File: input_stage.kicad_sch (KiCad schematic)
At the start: 35 parts, among them K1 EE2-3NUX, Q1 2N7002, U1 REF5030AD, U2 TL072, U6 NCS21802DMR2G, U7 CD4051B

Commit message: tiny.
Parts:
- added R29: 100k, Resistor_SMD:R_0603_1608Metric_Pad0.98x0.95mm_HandSolder, symbol Device:R_US
- R1, R10, R11, R2, R3, R4, R5, R7, R8, R9: footprint (none) -> Resistor_SMD:R_1206_3216Metric_Pad1.30x1.75mm_HandSolder
- R12, R13, R14, R15, R16, R17, R22, R23, R24, R25, R26, R27, R6: footprint (none) -> Resistor_SMD:R_0603_1608Metric_Pad0.98x0.95mm_HandSolder
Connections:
- net GND: now also R29.1
- net at R3.1: now also R5.1; no longer R2.1
- net at R8.1: now also R10.1; no longer R2.2
- net at Q1.1 (G), R14.1: now also R29.2
- net at R4.1: now also R3.2; no longer R5.1
- net at R5.2: now also R7.1; no longer R11.1
- net at R7.2: now also R9.2; no longer R8.2
- net at R9.1: now also R8.2; no longer R3.2
- net at R10.2: now also R11.1; no longer R9.2
- net at R4.2: now also R2.2; no longer R10.1
- net at R1.2: now also R2.1; no longer R7.1
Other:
- moved on the sheet: R14

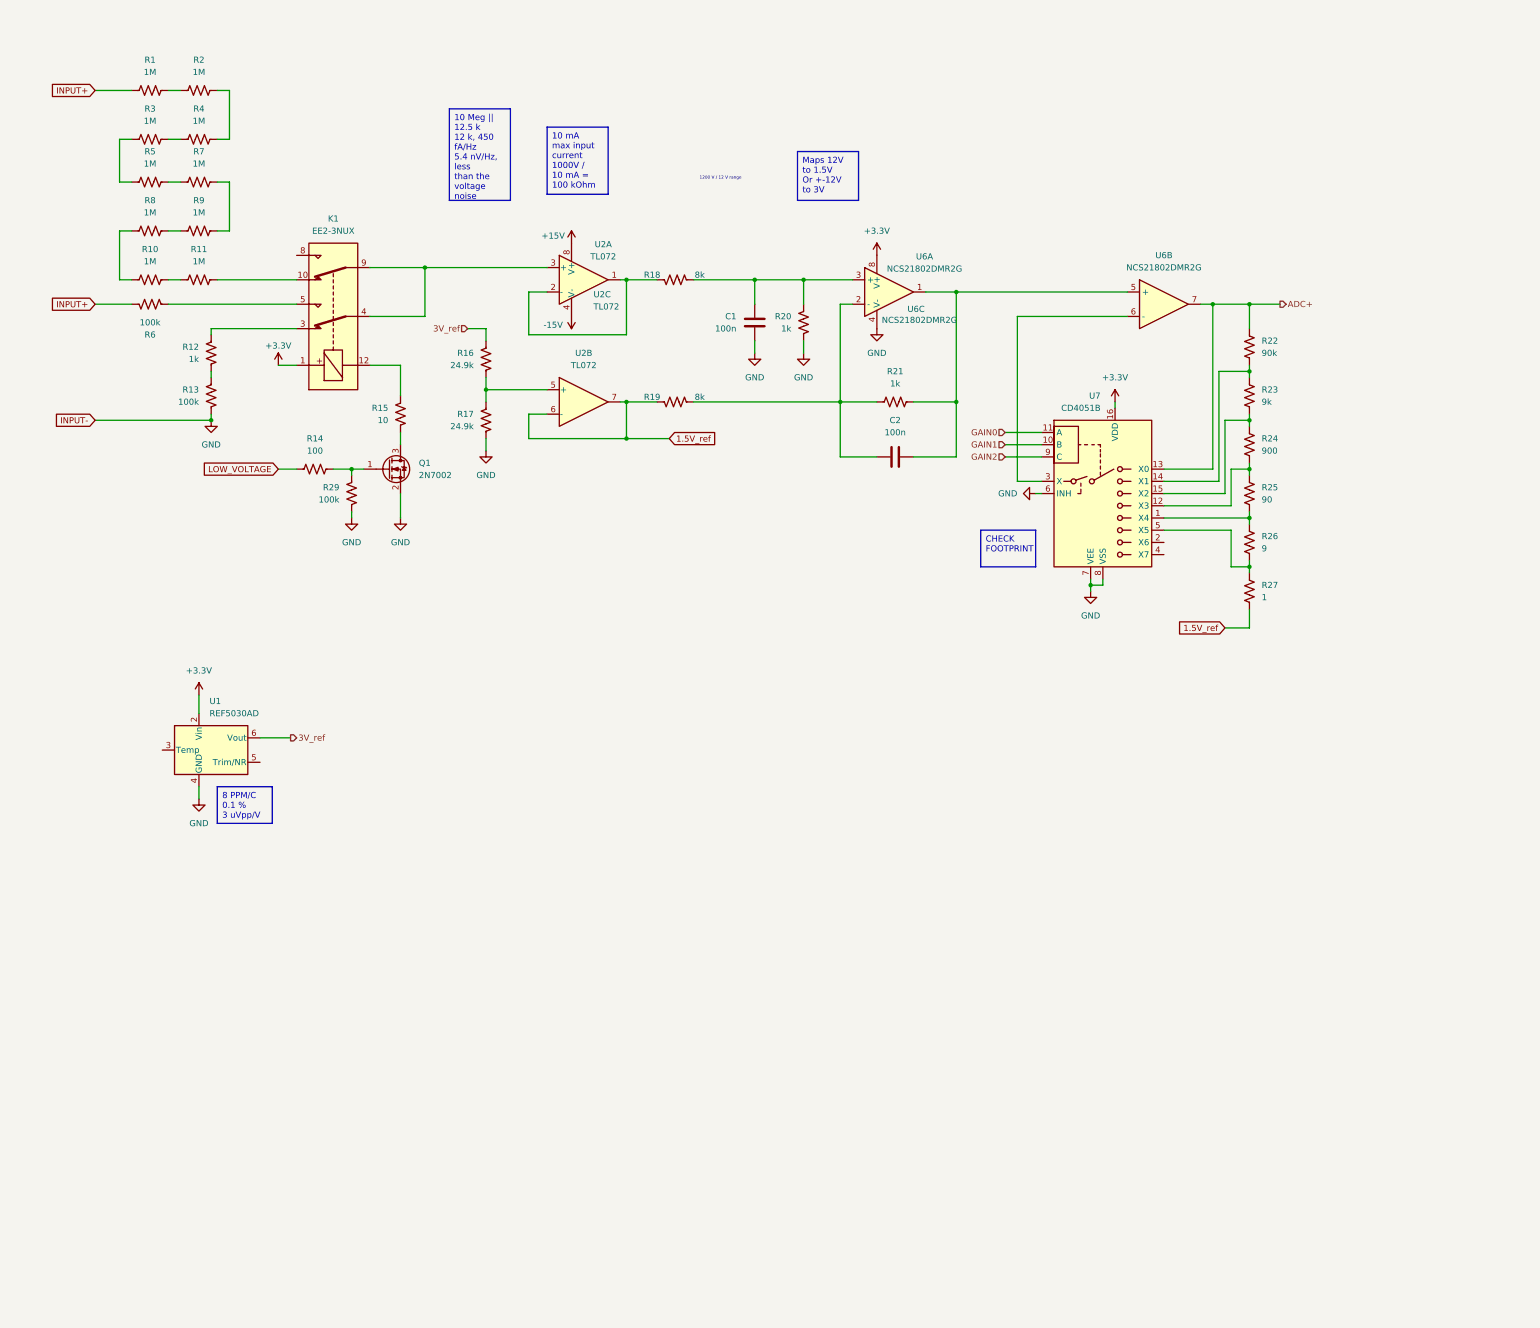
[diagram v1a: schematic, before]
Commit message: Added temperature, ref trimming and range selection resisitors.
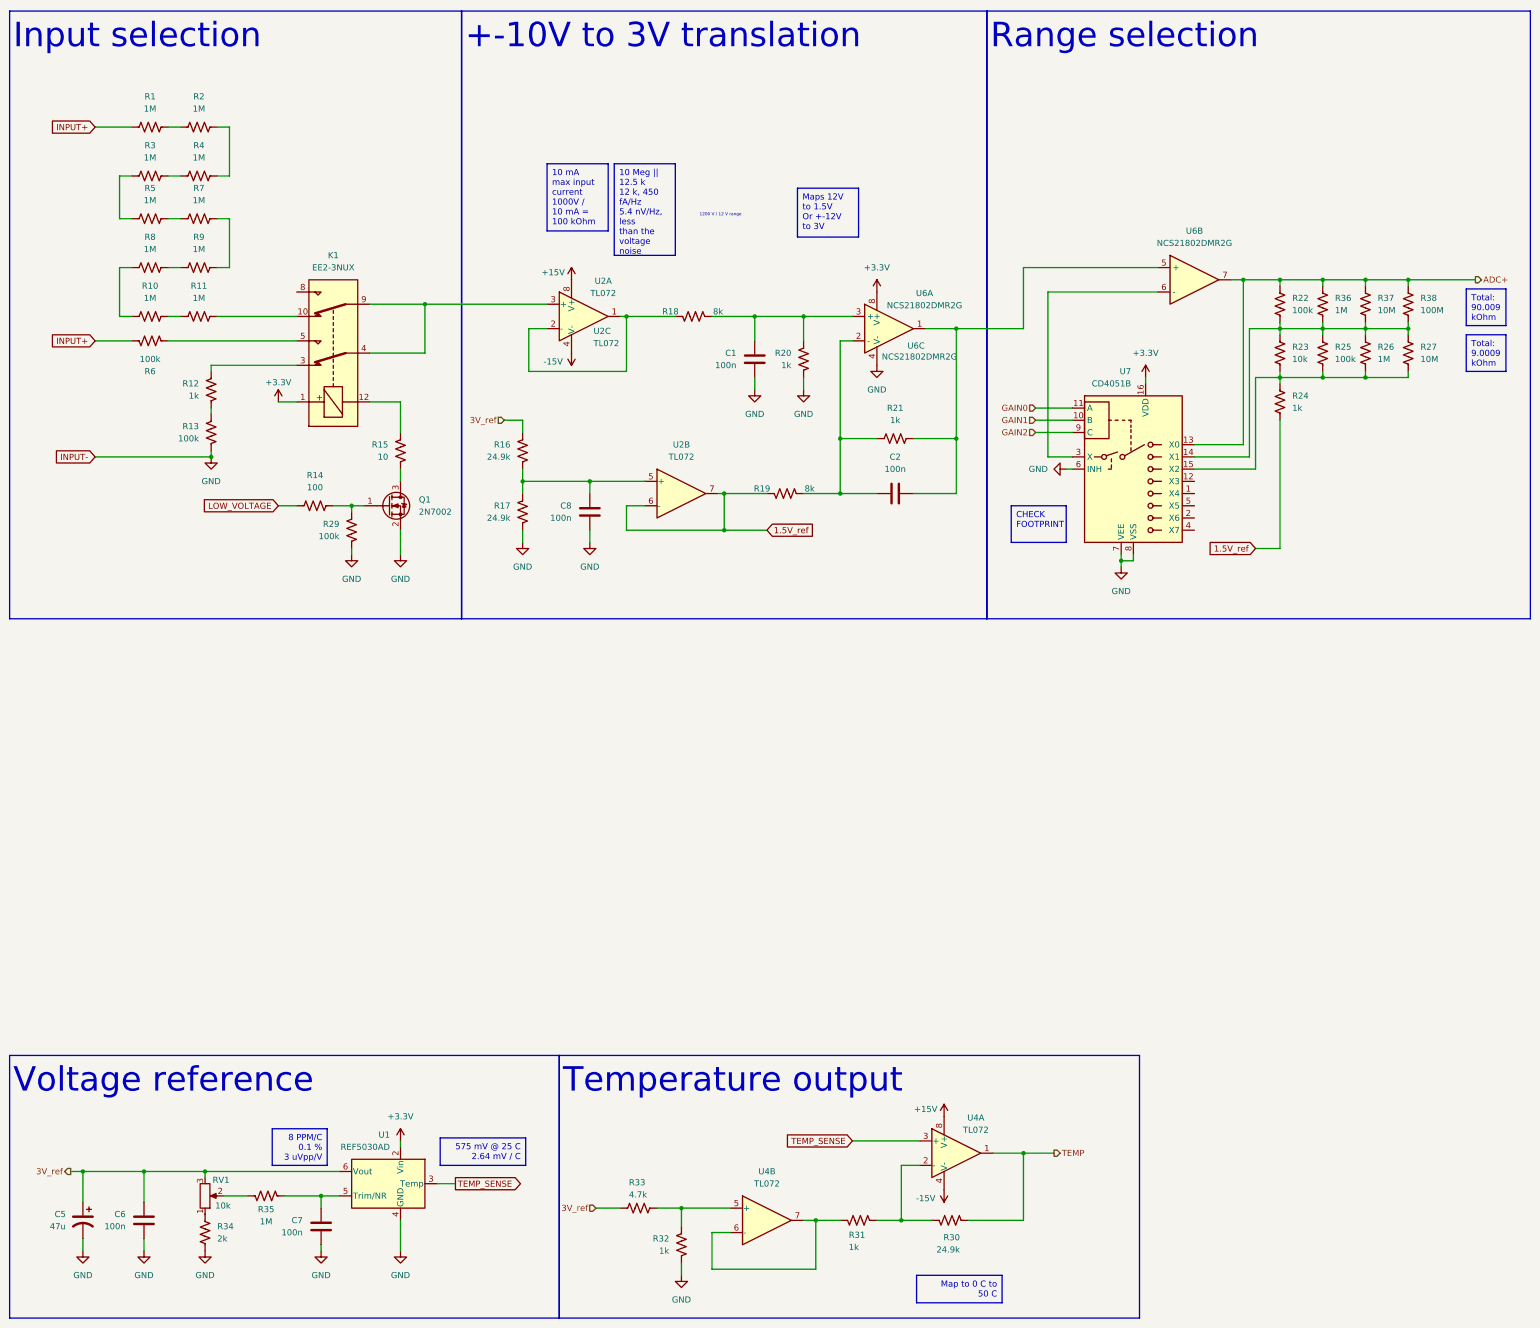
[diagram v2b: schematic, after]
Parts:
- added C5: 47u, Capacitor_THT:CP_Radial_D5.0mm_P2.00mm, symbol Device:C_Polarized_US
- added C6, C7, C8: 100n, Capacitor_SMD:C_0603_1608Metric_Pad1.08x0.95mm_HandSolder, symbol Device:C
- added R30: 24.9k, Resistor_SMD:R_0603_1608Metric_Pad0.98x0.95mm_HandSolder, symbol Device:R_US
- added R31, R32: 1k, Resistor_SMD:R_0603_1608Metric_Pad0.98x0.95mm_HandSolder, symbol Device:R_US
- added R33: 4.7k, Resistor_SMD:R_0603_1608Metric_Pad0.98x0.95mm_HandSolder, symbol Device:R_US
- added R34: 2k, Resistor_SMD:R_0603_1608Metric_Pad0.98x0.95mm_HandSolder, symbol Device:R_US
- added R35, R36: 1M, Resistor_SMD:R_0603_1608Metric_Pad0.98x0.95mm_HandSolder, symbol Device:R_US
- added R37: 10M, Resistor_SMD:R_0603_1608Metric_Pad0.98x0.95mm_HandSolder, symbol Device:R_US
- added R38: 100M, Resistor_SMD:R_0603_1608Metric_Pad0.98x0.95mm_HandSolder, symbol Device:R_US
- added RV1: 10k, Potentiometer_THT:Potentiometer_Bourns_3296W_Vertical, symbol Device:R_Potentiometer
- added U4: TL072, Package_SO:SOIC-8_3.9x4.9mm_P1.27mm, symbol Amplifier_Operational:TL072
- R22: value 90k -> 100k
- R23: value 9k -> 10k
- R24: value 900 -> 1k
- R25: value 90 -> 100k
- R26: value 9 -> 1M
- R27: value 1 -> 10M
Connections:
- net +15V: now also U4.8 (V+)
- net -15V: now also U4.4 (V-)
- net 1.5V_ref: now also R24.1; no longer R27.1
- net 3V_ref: now also C5.1, C6.2, R33.1, RV1.3
- net ADC+: now also R36.2, R37.2, R38.2
- net GND: now also C5.2, C6.1, C7.1, C8.1, R32.1, R34.1
- net at R22.1, R23.2, U7.14 (X1): now also R25.2, R26.2, R27.2, R36.1, R37.1, R38.1
- net at R23.1, R24.2, U7.15 (X2): now also R25.1, R26.1, R27.1
- net at R16.1, R17.2, U2.5 (+): now also C8.2
- net TEMP_SENSE: now reaches U1.3 (Temp)
- net TEMP_SENSE: now also U4.3 (+)
- net at U1.5 (Trim/NR): now also C7.2, R35.1
- new net: R30.2, R31.2, U4.2 (-)
- new net: R32.2, R33.2, U4.5 (+)
- new net: R31.1, U4.6 (-), U4.7
- new net: R34.2, RV1.1
- new net: R35.2, RV1.2
- new net TEMP: R30.1, U4.1
- now unconnected: U7.1 (X4), U7.12 (X3), U7.5 (X5)
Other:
- note added: "+-10V to 3V translation"
- note added: "Input selection"
- note added: "Range selection"
- note added: "Temperature output"
- note added: "Voltage reference"
- moved on the sheet: C1, C2, K1, Q1, R1, R10, R11, R12, R13, R14, R15, R16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

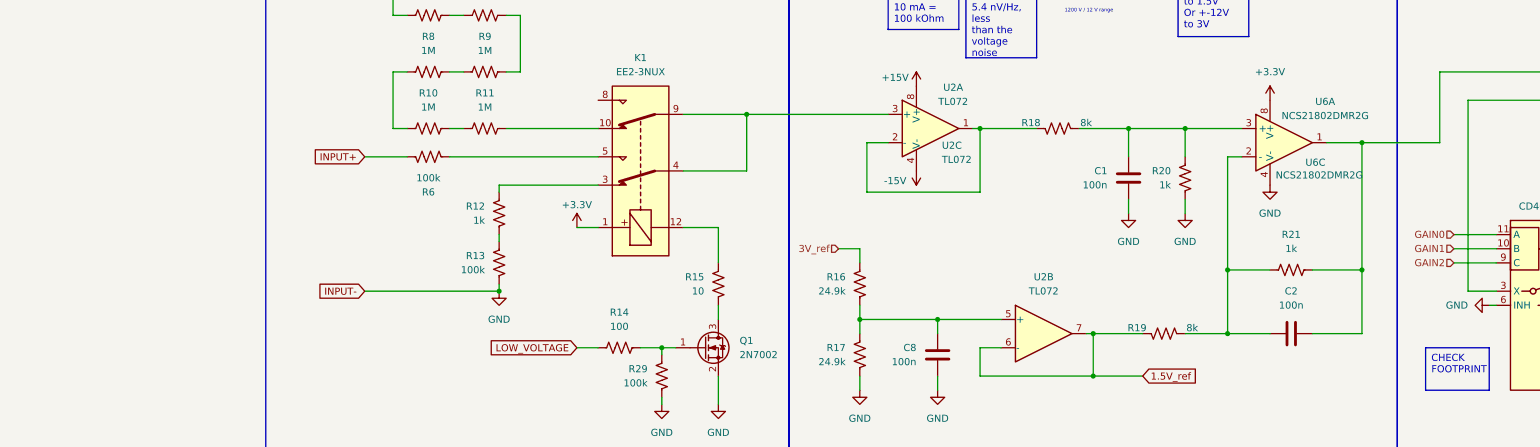
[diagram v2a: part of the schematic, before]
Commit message: Fixed diff amp.
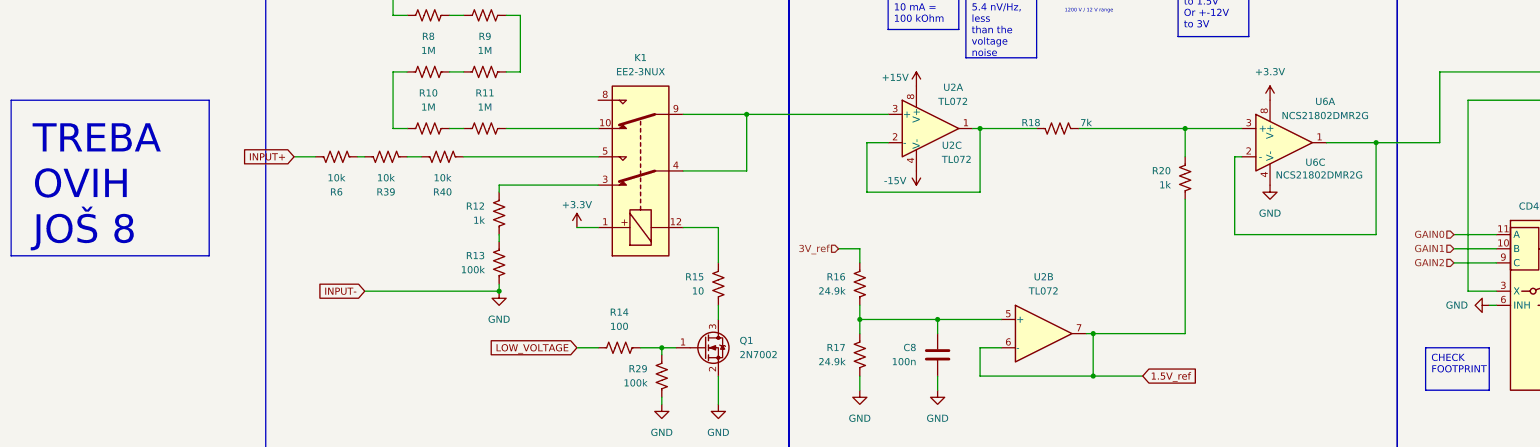
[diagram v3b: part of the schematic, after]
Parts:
- removed C1, C2: 100n, Capacitor_SMD:C_0603_1608Metric_Pad1.08x0.95mm_HandSolder, symbol Device:C
- removed R19: 8k, Resistor_SMD:R_0603_1608Metric_Pad0.98x0.95mm_HandSolder, symbol Device:R_US
- removed R21: 1k, Resistor_SMD:R_0603_1608Metric_Pad0.98x0.95mm_HandSolder, symbol Device:R_US
- added R39, R40: 10k, Resistor_SMD:R_0603_1608Metric_Pad0.98x0.95mm_HandSolder, symbol Device:R_US
- R18: value 8k -> 7k
- R6: value 100k -> 10k
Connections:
- net 1.5V_ref: now also R20.1
- net GND: no longer R20.1
- net at U6.1, U6.5 (+): now also U6.2 (-)
- net at K1.5: now also R40.1; no longer R6.1
- new net: R39.1, R40.2
- new net: R39.2, R6.1
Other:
- moved on the sheet: R6

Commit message: Recheck
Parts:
- added R19, R21, R41, R42, R43, R44, R45: 100k, Resistor_SMD:R_0603_1608Metric_Pad0.98x0.95mm_HandSolder, symbol Device:R_US
- R39, R40, R6: value 10k -> 100k
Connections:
- net INPUT+: now also R45.2; no longer R6.2
- net at R40.1: now also R21.1; no longer K1.5
- net at R39.1: now also R21.2; no longer R40.2
- net at R6.1: now also K1.8; no longer R39.2
- new net: R19.1, R6.2
- new net: R19.2, R39.2
- new net: R40.2, R41.1
- new net: R41.2, R43.2
- new net: R42.2, R43.1
- new net: R42.1, R44.1
- new net: R44.2, R45.1
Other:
- moved on the sheet: R18

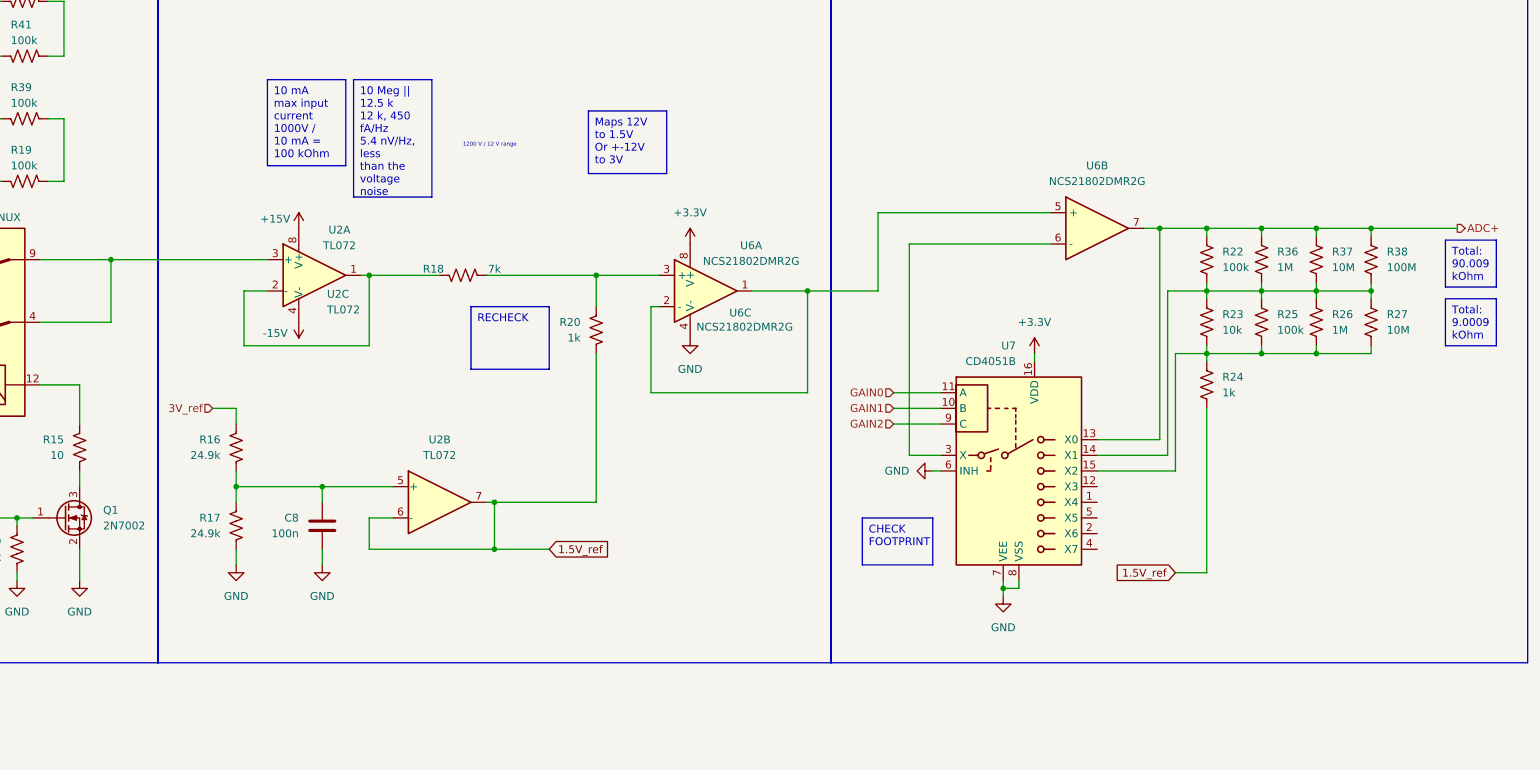
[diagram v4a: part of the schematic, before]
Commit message: Improved gain stage.
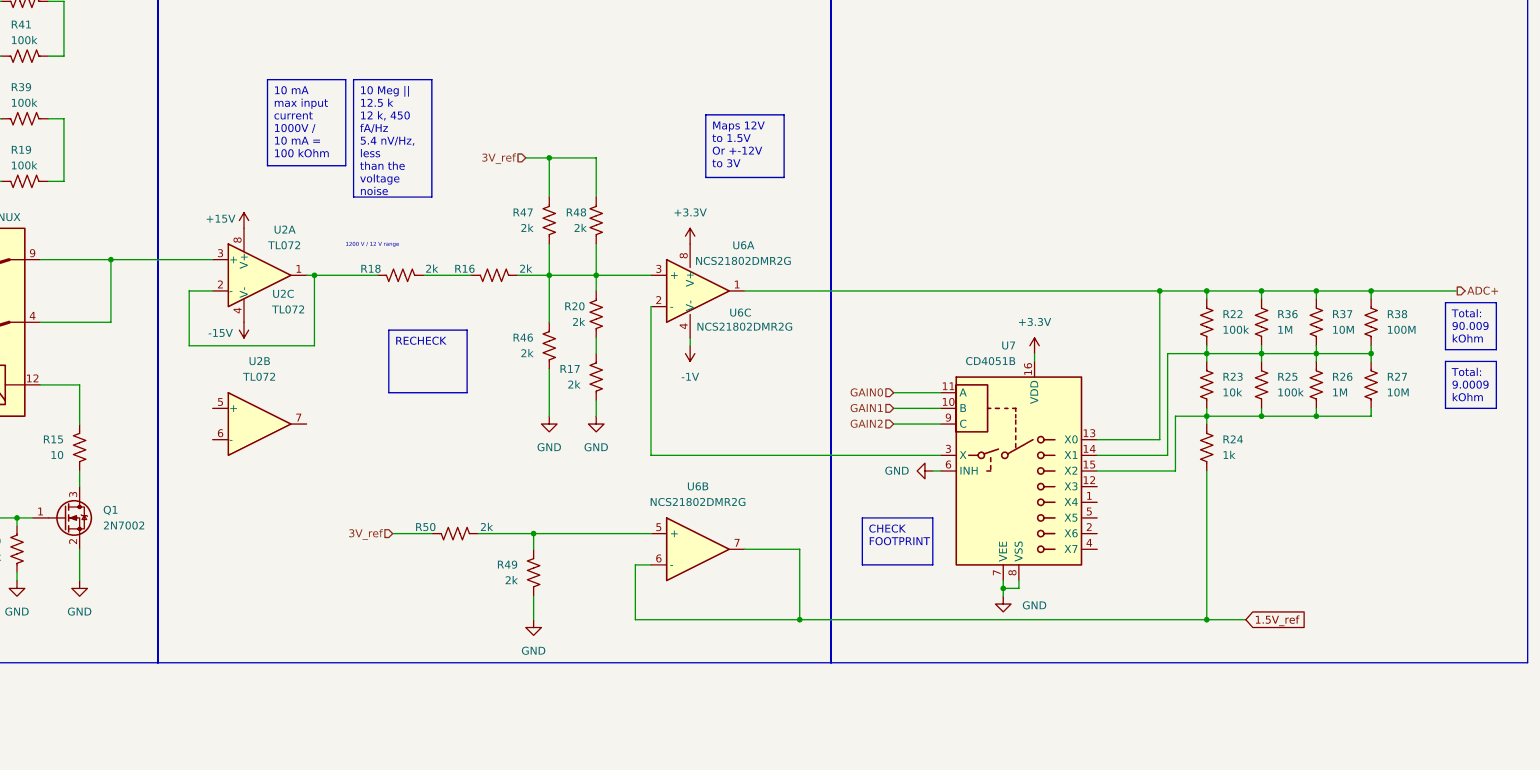
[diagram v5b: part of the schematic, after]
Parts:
- removed C8: 100n, Capacitor_SMD:C_0603_1608Metric_Pad1.08x0.95mm_HandSolder, symbol Device:C
- added R46, R47, R48, R49, R50: 2k, Resistor_SMD:R_0603_1608Metric_Pad0.98x0.95mm_HandSolder, symbol Device:R_US
- R16, R17: value 24.9k -> 2k
- R18: value 7k -> 2k
- R20: value 1k -> 2k
- U2: footprint Package_SO:SOIC-8_3.9x4.9mm_P1.27mm -> (none)
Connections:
- net 1.5V_ref: now also U6.6 (-), U6.7; no longer R20.1, U2.6 (-), U2.7
- net 3V_ref: now also R47.2, R48.2, R50.2; no longer R16.2
- net ADC+: now also U6.1; no longer U6.7
- net GND: now also R46.1, R49.1; no longer U6.4 (V-)
- net at U7.3 (X): now also U6.2 (-); no longer U6.6 (-)
- net at R20.2, U6.3 (+): now also R16.1, R46.2, R47.1, R48.1; no longer R18.1
- new net: R49.2, R50.1, U6.5 (+)
- new net: R16.2, R18.1
- new net: R17.2, R20.1
- new net -1V: U6.4 (V-)
- now unconnected: U2.5 (+)
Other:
- moved on the sheet: R18, R20, R22, R23, R24, R25, R26, R27, R36, R37, R38, U2A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

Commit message: sqrt2 noise
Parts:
- added R51, R52: 4k, Resistor_SMD:R_0603_1608Metric_Pad0.98x0.95mm_HandSolder, symbol Device:R_US
- R16, R18: value 2k -> 4k
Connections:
- net at U2.5 (+): now also K1.4, K1.9, U2.3 (+)
- net at U2.6 (-): now also U2.7, R51.2
- net at R16.1, R20.2, R46.2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: now also R52.1
- new net: R51.1, R52.2
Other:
- moved on the sheet: R16, R18
